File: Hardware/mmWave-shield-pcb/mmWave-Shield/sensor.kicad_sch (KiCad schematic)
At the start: 27 parts, among them U1 KC2016K80.0000C1GE00

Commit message: kicad project inital version
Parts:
- FB1, FB2, FB3, FB4, FB5, FB6, FB7: footprint Inductor_SMD:L_01005_0402Metric -> MMZ1005S121CT000:IND_1005_TDK-L
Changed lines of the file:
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@@
 			)
 		)
-		(property "Footprint" "Inductor_SMD:L_01005_0402Metric"
+		(property "Footprint" "MMZ1005S121CT000:IND_1005_TDK-L"
 			(at 80.01 164.338 90)
 			(effects
@@
 			)
 		)
-		(property "Footprint" "Inductor_SMD:L_01005_0402Metric"
+		(property "Footprint" "MMZ1005S121CT000:IND_1005_TDK-L"
 			(at 127 136.398 90)
 			(effects
@@
 			)
 		)
-		(property "Footprint" "Inductor_SMD:L_01005_0402Metric"
+		(property "Footprint" "MMZ1005S121CT000:IND_1005_TDK-L"
 			(at 254 37.338 90)
 			(effects
@@
 			)
 		)
-		(property "Footprint" "Inductor_SMD:L_01005_0402Metric"
+		(property "Footprint" "MMZ1005S121CT000:IND_1005_TDK-L"
 			(at 80.01 136.398 90)
 			(effects
@@
 			)
 		)
-		(property "Footprint" "Inductor_SMD:L_01005_0402Metric"
+		(property "Footprint" "MMZ1005S121CT000:IND_1005_TDK-L"
 			(at 40.64 164.338 90)
 			(effects
@@
 			)
 		)
-		(property "Footprint" "Inductor_SMD:L_01005_0402Metric"
+		(property "Footprint" "MMZ1005S121CT000:IND_1005_TDK-L"
 			(at 121.92 164.338 90)
 			(effects
@@
 			)
 		)
-		(property "Footprint" "Inductor_SMD:L_01005_0402Metric"
+		(property "Footprint" "MMZ1005S121CT000:IND_1005_TDK-L"
 			(at 40.64 136.398 90)
 			(effects

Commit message: working on scematic1
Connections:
- net SPI_A_CS renamed SPI_CSN
- no-connect marks 5 -> 1
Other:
- note removed: "Needs to be inverted or use other GPIO pin?"
- note removed: "Test points/ half circles around the edge like dev board?"
- note removed: "Which? also spi A or B"

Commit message: Placed Connectors in hopefully right way
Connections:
- net IRQ renamed nRF_P0.05
- net RST renamed nRF_P0.04
- net SPI_CSN renamed nRF_P0.07/AMUX
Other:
- note added: "80 MHz Clock gen"
- note added: "Decoupling"
- note added: "To connectors"
- moved on the sheet: C10, C11, C12, C13, C14, C15, C16, C2, C3, C4, C5, C6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

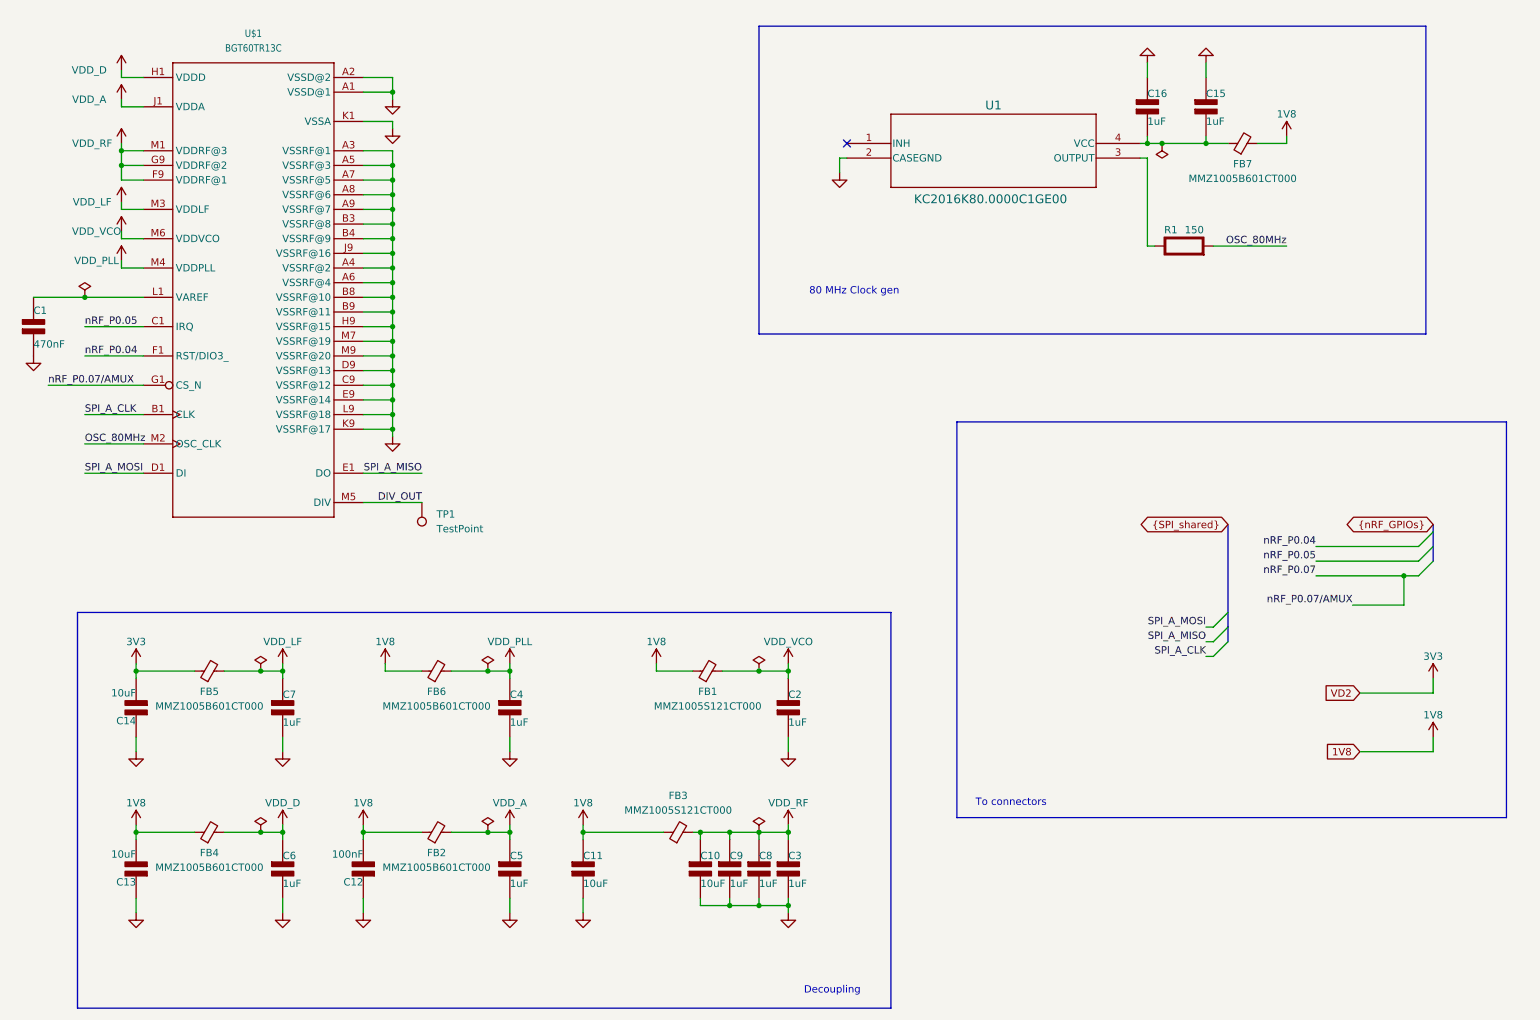
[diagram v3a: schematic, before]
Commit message: small changes scematic
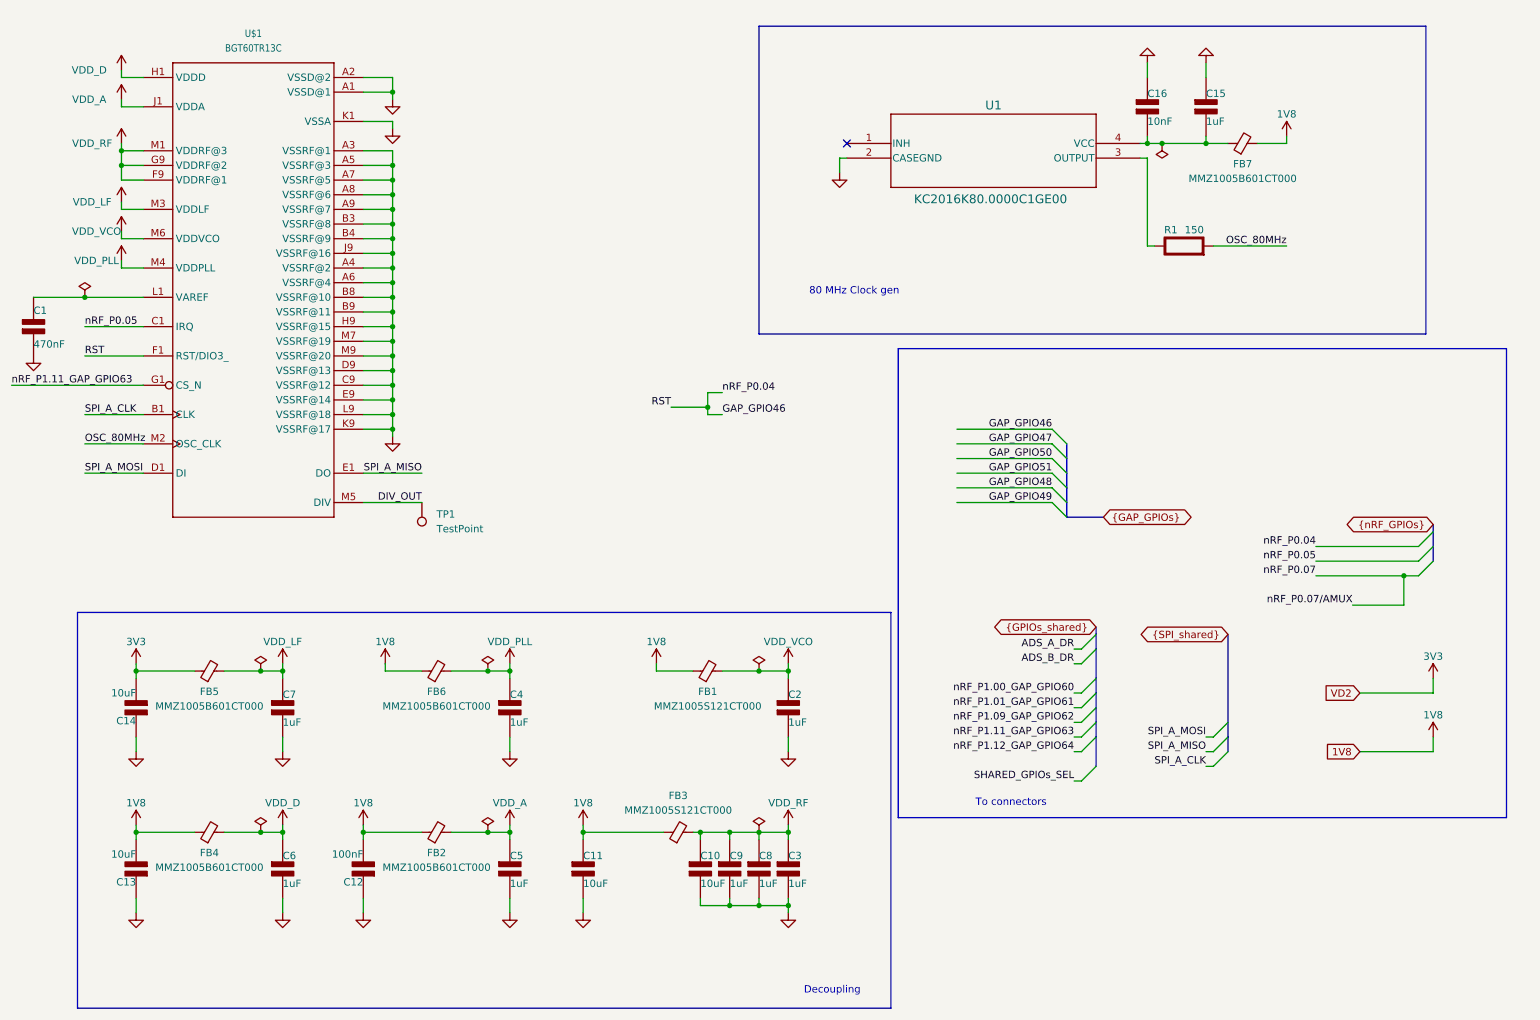
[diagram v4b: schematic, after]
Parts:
- C16: value 1uF -> 10nF
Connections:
- net nRF_P0.04 renamed GAP_GPIO46
- net nRF_P0.07/AMUX renamed nRF_P1.11_GAP_GPIO63

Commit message: V1 of pcb layout
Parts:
- TP1: footprint TestPoint:TestPoint_Pad_D1.5mm -> TestPoint:TestPoint_Pad_D1.0mm
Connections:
- net nRF_P0.05 renamed nRF_P0.12_GAP_GPIO64
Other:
- note removed: "To connectors"
- moved on the sheet: C1, C15, C16, FB7, R1, TP1, U$1, U1

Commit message: small adjustments
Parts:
- added R3, R4: 0ohm, Resistor_SMD:R_0805_2012Metric, symbol PCM_SL_Resistors:0ohm
- added U1, U2: TPS22916CYFPR, aaEXTRAS:TPS22916CYFPR, symbol KC2016K80:TPS22916CYFPR
- renumbered U1 to X1
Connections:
- net 1V8: now also U1.A1 (VOUT)
- net 3V3: now also U2.A1 (VOUT)
- net GND: now also U1.B1 (GND), U2.B1 (GND)
- new net: R4.1, U2.A2 (VIN)
- new net: R3.1, U1.A2 (VIN)
- new net 1V8_Connector: R3.2
- new net VD2: R4.2
- new net nRF_P0.07/AMUX: U1.B2 (ON), U2.B2 (ON)
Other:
- note added: "GPIO NEEDS TO BE CONFIGURED HIGH"

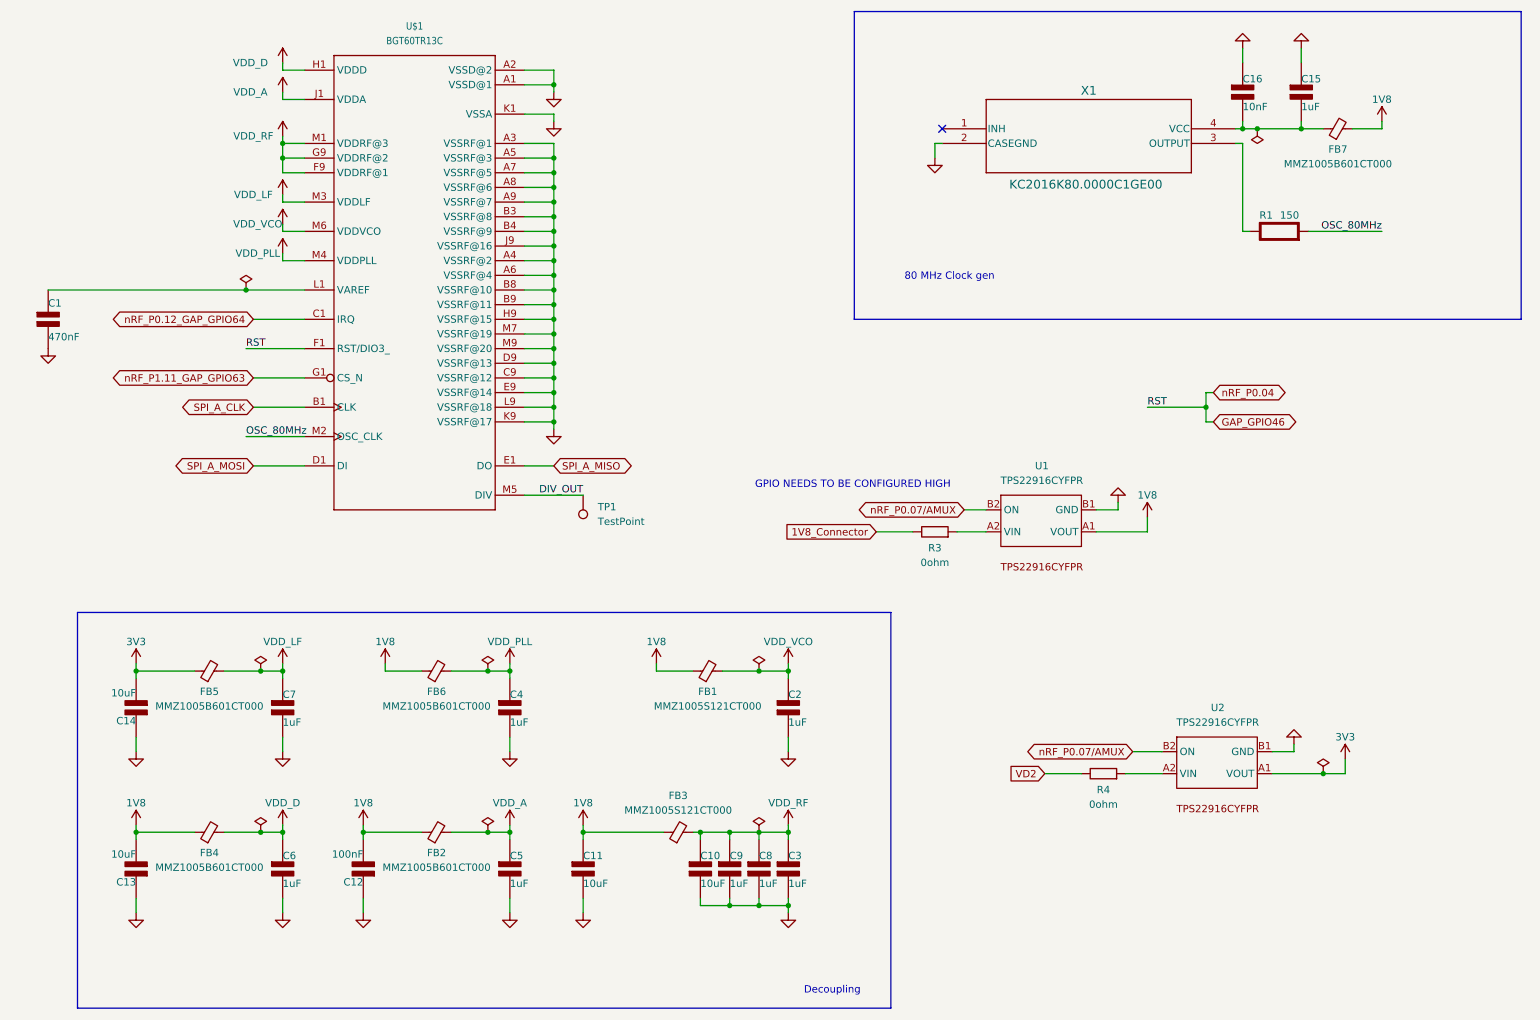
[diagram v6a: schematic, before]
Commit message: finished adding power controll
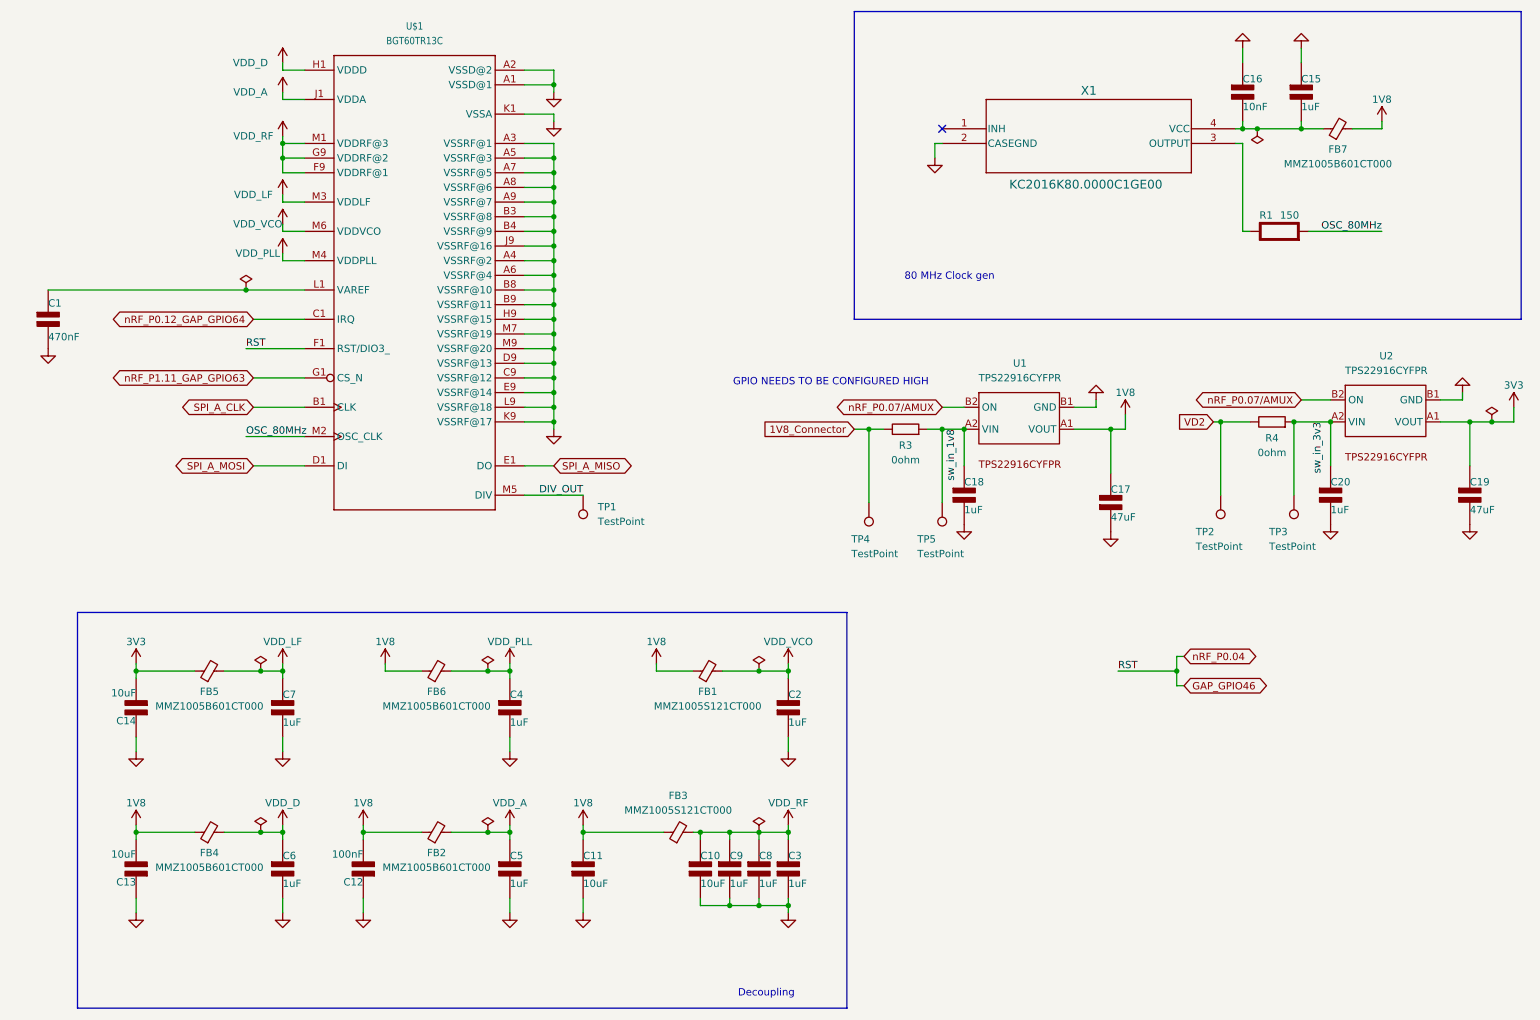
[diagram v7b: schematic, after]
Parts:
- added C17, C19: 47uF, Capacitor_SMD:C_0402_1005Metric, symbol PCM_Elektuur:C
- added C18, C20: 1uF, Capacitor_SMD:C_0402_1005Metric, symbol PCM_Elektuur:C
- added TP2, TP3, TP4, TP5: TestPoint, TestPoint:TestPoint_Pad_D1.0mm, symbol Connector:TestPoint
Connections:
- net 1V8: now also C17.1 (+)
- net 1V8_Connector: now also TP4.1
- net 3V3: now also C19.1 (+)
- net GND: now also C17.2 (-), C18.2 (-), C19.2 (-), C20.2 (-)
- net VD2: now also TP2.1
- net sw_in_3v3: now reaches R4.1, U2.A2 (VIN)
- net sw_in_3v3: now also C20.1 (+), TP3.1
- net sw_in_1v8: now reaches R3.1, U1.A2 (VIN)
- net sw_in_1v8: now also C18.1 (+), TP5.1
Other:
- moved on the sheet: R3, R4, U1, U2

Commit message: changed schema
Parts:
- removed C17, C19: 47uF, Capacitor_SMD:C_0402_1005Metric, symbol PCM_Elektuur:C
- C18, C20: value 1uF -> 4.7uF
